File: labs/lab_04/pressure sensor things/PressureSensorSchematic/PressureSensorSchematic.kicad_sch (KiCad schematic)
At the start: 11 parts, among them U1 MCP601-xSN, U2 MPXA6115A

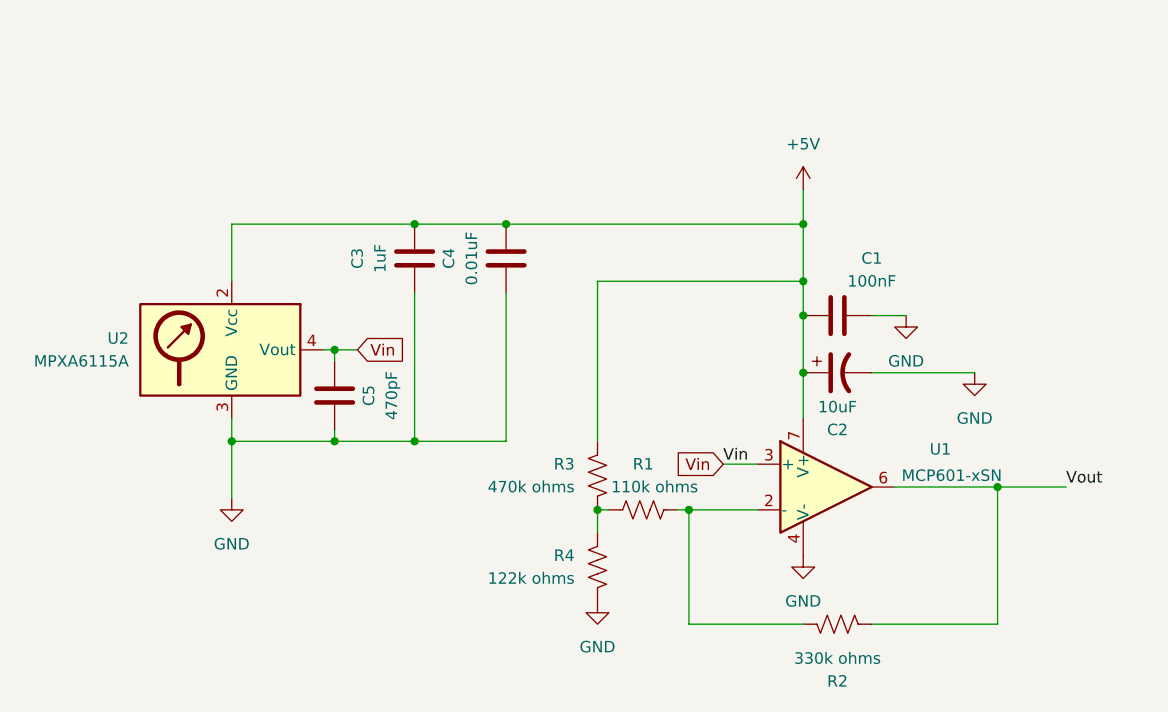
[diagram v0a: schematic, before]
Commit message: Clean up schematic
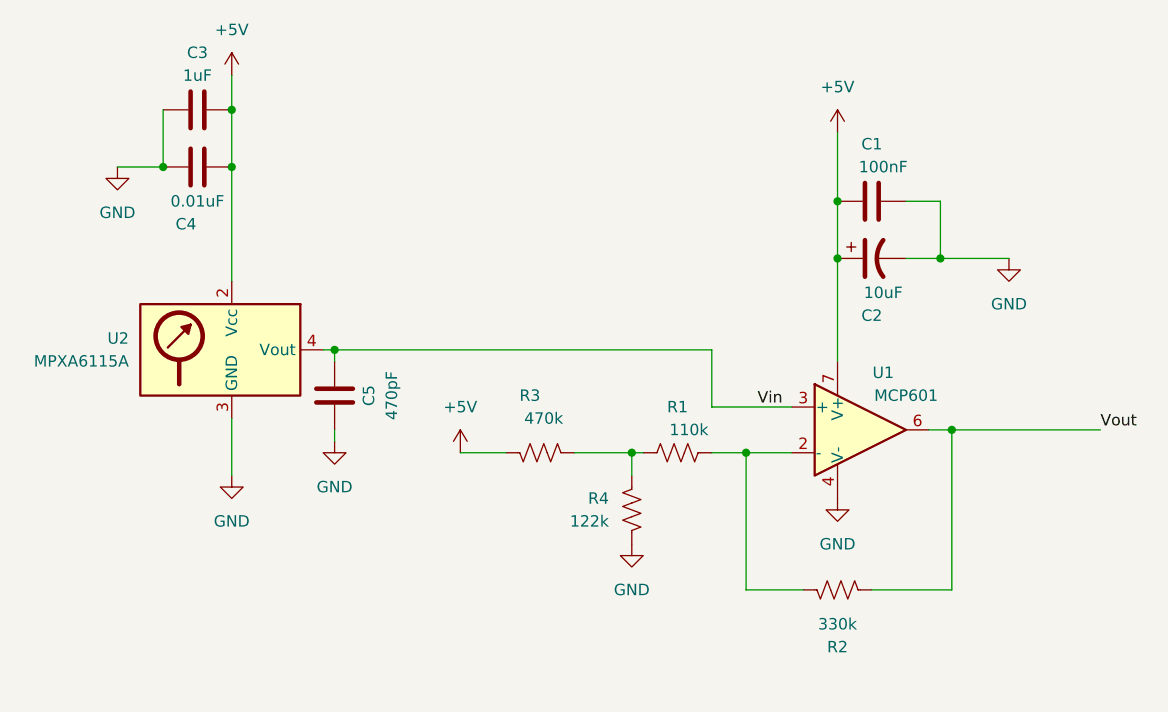
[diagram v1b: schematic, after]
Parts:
- R1: value 110k ohms -> 110k
- R2: value 330k ohms -> 330k
- R3: value 470k ohms -> 470k
- R4: value 122k ohms -> 122k
- U1: value MCP601-xSN -> MCP601
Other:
- moved on the sheet: C1, C2, C3, C4, R1, R2, R3, R4, U1
